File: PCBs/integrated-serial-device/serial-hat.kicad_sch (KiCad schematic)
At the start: 24 parts, among them CN1 Modem port, CN2 Modem out 3, CN3 Printer port, J1 Rpi headers, J2 Conn_01x03_Pin, K1 Quicktake, K2 ImageWriter, SW1 Modem To Proxy, SW2 Modem to Quicktake, SW3 Modem out 3, SW4 Printer out 3, SW5 Printer to Proxy, SW6 Printer to ImageWriter, SW7 SW_SPST, U1 MAX3232

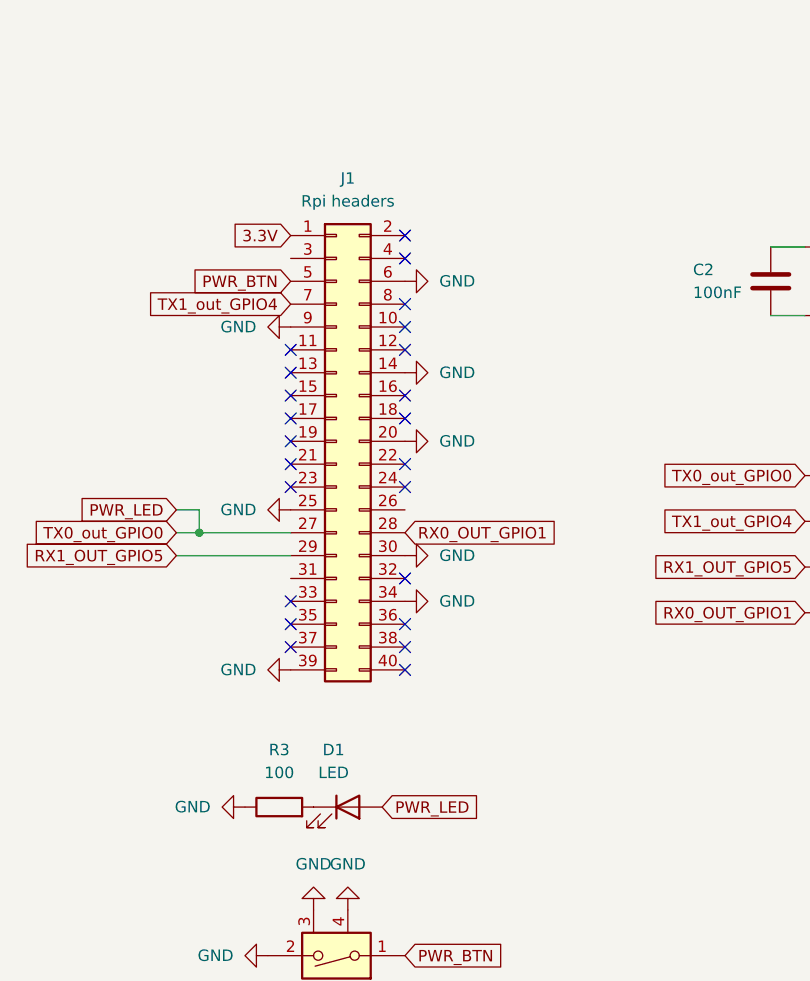
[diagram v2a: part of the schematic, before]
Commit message: Add fan headers
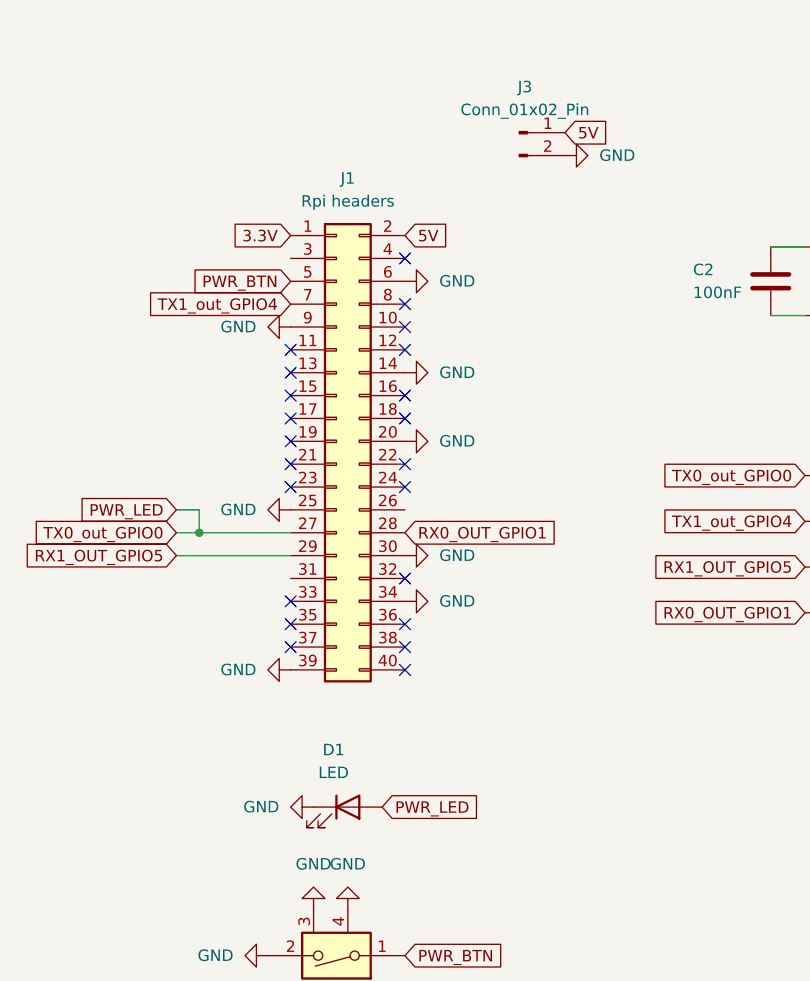
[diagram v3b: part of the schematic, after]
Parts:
- removed R3: 100, Resistor_SMD:R_0603_1608Metric, symbol Device:R
- added J3: Conn_01x02_Pin, Connector_PinHeader_2.54mm:PinHeader_1x02_P2.54mm_Vertical, symbol Connector:Conn_01x02_Pin
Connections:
- net GND: now also D1.1 (K), J3.2 (Pin_2)
- net 5V: now reaches J1.2 (Pin_2)
- net 5V: now also J3.1 (Pin_1)
- no-connect marks 59 -> 58
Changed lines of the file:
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@@
 	)
 	(no_connect
-		(at 100.33 38.1)
+		(at 100.33 40.64)
 	)
 	(no_connect
@@
 	)
 	(no_connect
-		(at 100.33 40.64)
-	)
-	(no_connect
 		(at 261.62 148.59)
 	)
@@
 		)
 	)
+	(global_label "5V"
+		(shape input)
+		(at 100.33 38.1 0)
+		(fields_autoplaced yes)
+		(effects
+			(font
+				(size 1.27 1.27)
+			)
+			(justify left)
+		)
+		(property "Intersheetrefs" "${INTERSHEET_REFS}"
+			(at 105.6133 38.1 0)
+			(effects
+				(font
+					(size 1.27 1.27)
+				)
+				(justify left)
+				(hide yes)
+			)
+		)
+	)
 	(global_label "IW_DSR"
 		(shape input)
@@
 		)
 	)
+	(global_label "5V"
+		(shape input)
+		(at 118.11 26.67 0)
+		(fields_autoplaced yes)
+		(effects
+			(font
+				(size 1.27 1.27)
+			)
+			(justify left)
+		)
+		(property "Intersheetrefs" "${INTERSHEET_REFS}"
+			(at 123.3933 26.67 0)
+			(effects
+				(font
+					(size 1.27 1.27)
+				)
+				(justify left)
+				(hide yes)
+			)
+		)
+	)
 	(global_label "IW_TX"
 		(shape input)
@@
 	)
 	(symbol
+		(lib_id "Connector:Conn_01x02_Pin")
+		(at 113.03 26.67 0)
+		(unit 1)
+		(exclude_from_sim no)
+		(in_bom yes)
+		(on_board yes)
+		(dnp no)
+		(fields_autoplaced yes)
+		(property "Reference" "J3"
+			(at 113.665 21.59 0)
+			(effects
+				(font
+					(size 1.27 1.27)
+				)
+			)
+		)
+		(property "Value" "Conn_01x02_Pin"
+			(at 113.665 24.13 0)
+			(effects
+				(font
+					(size 1.27 1.27)
+				)
+			)
+		)
+		(property "Footprint" "Connector_PinHeader_2.54mm:PinHeader_1x02_P2.54mm_Vertical"
+			(at 113.03 26.67 0)
+			(effects
+				(font
+					(size 1.27 1.27)
+				)
+				(hide yes)
+			)
+		)
+		(property "Datasheet" "~"
+			(at 113.03 26.67 0)
+			(effects
+				(font
+					(size 1.27 1.27)
+				)
+				(hide yes)
+			)
+		)
+		(property "Description" "Generic connector, single row, 01x02, script generated"
+			(at 113.03 26.67 0)
+			(effects
+				(font
+					(size 1.27 1.27)
+				)
+				(hide yes)
+			)
+		)
+		(pin "1"
+		)
+		(pin "2"
+		)
+		(instances
+			(project "serial-hat"
+				(path "/f30a5902-bf77-48c6-ab50-b8e2235ec207"
+					(reference "J3")
+					(unit 1)
+				)
+			)
+		)
+	)
+	(symbol
 		(lib_id "Device:R_US")
 		(at 189.23 74.93 90)
@@
 	)
 	(symbol
+		(lib_id "power:GND")
+		(at 118.11 29.21 90)
+		(unit 1)
+		(exclude_from_sim no)
+		(in_bom yes)
+		(on_board yes)
+		(dnp no)
+		(fields_autoplaced yes)
+		(property "Reference" "#PWR032"
+			(at 124.46 29.21 0)
+			(effects
+				(font
+					(size 1.27 1.27)
+				)
+				(hide yes)
+			)
+		)
+		(property "Value" "GND"
+			(at 121.92 29.2099 90)
+			(effects
+				(font
+					(size 1.27 1.27)
+				)
+				(justify right)
+			)
+		)
+		(property "Footprint" ""
+			(at 118.11 29.21 0)
+			(effects
+				(font
+					(size 1.27 1.27)
+				)
+				(hide yes)
+			)
+		)
+		(property "Datasheet" ""
+			(at 118.11 29.21 0)
+			(effects
+				(font
+					(size 1.27 1.27)
+				)
+				(hide yes)
+			)
+		)
+		(property "Description" "Power symbol creates a global label with name \"GND\" , ground"
+			(at 118.11 29.21 0)
+			(effects
+				(font
+					(size 1.27 1.27)
+				)
+				(hide yes)
+			)
+		)
+		(pin "1"
+		)
+		(instances
+			(project "serial-hat"
+				(path "/f30a5902-bf77-48c6-ab50-b8e2235ec207"
+					(reference "#PWR032")
+					(unit 1)
+				)
+			)
+		)
+	)
+	(symbol
 		(lib_id "Device:C")
 		(at 140.97 43.18 0)
@@
 	)
 	(symbol
-		(lib_id "Device:R")
-		(at 86.36 101.6 90)
-		(unit 1)
-		(exclude_from_sim no)
-		(in_bom yes)
-		(on_board yes)
-		(dnp no)
-		(fields_autoplaced yes)
-		(property "Reference" "R3"
-			(at 86.36 95.25 90)
-			(effects
-				(font
-					(size 1.27 1.27)
-				)
-			)
-		)
-		(property "Value" "100"
-			(at 86.36 97.79 90)
-			(effects
-				(font
-					(size 1.27 1.27)
-				)
-			)
-		)
-		(property "Footprint" "Resistor_SMD:R_0603_1608Metric"
-			(at 86.36 103.378 90)
-			(effects
-				(font
-					(size 1.27 1.27)
-				)
-				(hide yes)
-			)
-		)
-		(property "Datasheet" "~"
-			(at 86.36 101.6 0)
-			(effects
-				(font
-					(size 1.27 1.27)
-				)
-				(hide yes)
-			)
-		)
-		(property "Description" "Resistor"
-			(at 86.36 101.6 0)
-			(effects
-				(font
-					(size 1.27 1.27)
-				)
-				(hide yes)
-			)
-		)
-		(property "LCSC" "C22775"
-			(at 86.36 101.6 90)
-			(effects
-				(font
-					(size 1.27 1.27)
-				)
-				(hide yes)
-			)
-		)
-		(pin "2"
-		)
-		(pin "1"
-		)
-		(instances
-			(project "serial-hat"
-				(path "/f30a5902-bf77-48c6-ab50-b8e2235ec207"
-					(reference "R3")
-					(unit 1)
-				)
-			)
-		)
-	)
-	(symbol
 		(lib_id "power:GND")
 		(at 255.27 142.24 90)
@@
 	(symbol
 		(lib_id "power:GND")
-		(at 82.55 101.6 270)
+		(at 90.17 101.6 270)
 		(unit 1)
 		(exclude_from_sim no)
@@
 		(fields_autoplaced yes)
 		(property "Reference" "#PWR029"
-			(at 76.2 101.6 0)
+			(at 83.82 101.6 0)
 			(effects
 				(font
@@
 		)
 		(property "Value" "GND"
-			(at 78.74 101.6001 90)
+			(at 86.36 101.6001 90)
 			(effects
 				(font
@@
 		)
 		(property "Footprint" ""
-			(at 82.55 101.6 0)
+			(at 90.17 101.6 0)
 			(effects
 				(font
@@
 		)
 		(property "Datasheet" ""
-			(at 82.55 101.6 0)
+			(at 90.17 101.6 0)
 			(effects
 				(font
@@
 		)
 		(property "Description" "Power symbol creates a global label with name \"GND\" , ground"
-			(at 82.55 101.6 0)
+			(at 90.17 101.6 0)
 			(effects
 				(font

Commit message: CISD ready
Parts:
- removed R1, R2: 3.3k, Resistor_SMD:R_0603_1608Metric, symbol Device:R_US
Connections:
- net A2_AUX_TTY_TX: now also U1.13 (R1IN)
- net A2_TTY_TX: now also U1.8 (R2IN)
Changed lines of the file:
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@@
 	(global_label "A2_AUX_TTY_TX"
 		(shape input)
-		(at 193.04 74.93 0)
-		(fields_autoplaced yes)
-		(effects
-			(font
-				(size 1.27 1.27)
-			)
-			(justify left)
-		)
-		(property "Intersheetrefs" "${INTERSHEET_REFS}"
-			(at 210.0556 74.93 0)
+		(at 185.42 74.93 0)
+		(fields_autoplaced yes)
+		(effects
+			(font
+				(size 1.27 1.27)
+			)
+			(justify left)
+		)
+		(property "Intersheetrefs" "${INTERSHEET_REFS}"
+			(at 202.4356 74.93 0)
 			(effects
 				(font
@@
 	(global_label "A2_TTY_TX"
 		(shape input)
-		(at 193.04 80.01 0)
-		(fields_autoplaced yes)
-		(effects
-			(font
-				(size 1.27 1.27)
-			)
-			(justify left)
-		)
-		(property "Intersheetrefs" "${INTERSHEET_REFS}"
-			(at 205.4594 80.01 0)
+		(at 185.42 80.01 0)
+		(fields_autoplaced yes)
+		(effects
+			(font
+				(size 1.27 1.27)
+			)
+			(justify left)
+		)
+		(property "Intersheetrefs" "${INTERSHEET_REFS}"
+			(at 197.8394 80.01 0)
 			(effects
 				(font
@@
 				(path "/f30a5902-bf77-48c6-ab50-b8e2235ec207"
 					(reference "J3")
-					(unit 1)
-				)
-			)
-		)
-	)
-	(symbol
-		(lib_id "Device:R_US")
-		(at 189.23 74.93 90)
-		(unit 1)
-		(exclude_from_sim no)
-		(in_bom yes)
-		(on_board yes)
-		(dnp no)
-		(property "Reference" "R1"
-			(at 187.452 72.898 90)
-			(effects
-				(font
-					(size 1.27 1.27)
-				)
-			)
-		)
-		(property "Value" "3.3k"
-			(at 192.278 72.898 90)
-			(effects
-				(font
-					(size 1.27 1.27)
-				)
-			)
-		)
-		(property "Footprint" "Resistor_SMD:R_0603_1608Metric"
-			(at 189.484 73.914 90)
-			(effects
-				(font
-					(size 1.27 1.27)
-				)
-				(hide yes)
-			)
-		)
-		(property "Datasheet" "~"
-			(at 189.23 74.93 0)
-			(effects
-				(font
-					(size 1.27 1.27)
-				)
-				(hide yes)
-			)
-		)
-		(property "Description" "Resistor, US symbol"
-			(at 189.23 74.93 0)
-			(effects
-				(font
-					(size 1.27 1.27)
-				)
-				(hide yes)
-			)
-		)
-		(property "LCSC" "C21190"
-			(at 189.23 74.93 90)
-			(effects
-				(font
-					(size 1.27 1.27)
-				)
-				(hide yes)
-			)
-		)
-		(pin "2"
-		)
-		(pin "1"
-		)
-		(instances
-			(project "serial-hat"
-				(path "/f30a5902-bf77-48c6-ab50-b8e2235ec207"
-					(reference "R1")
 					(unit 1)
 				)
@@
 					(unit 1)
 				)
-			)
-		)
-	)
-	(symbol
-		(lib_id "Device:R_US")
-		(at 189.23 80.01 90)
-		(unit 1)
-		(exclude_from_sim no)
-		(in_bom yes)
-		(on_board yes)
-		(dnp no)
-		(property "Reference" "R2"
-			(at 187.452 77.978 90)
-			(effects
-				(font
-					(size 1.27 1.27)
-				)
-			)
-		)
-		(property "Value" "3.3k"
-			(at 192.278 77.978 90)
-			(effects
-				(font
-					(size 1.27 1.27)
-				)
-			)
-		)
-		(property "Footprint" "Resistor_SMD:R_0603_1608Metric"
-			(at 189.484 78.994 90)
-			(effects
-				(font
-					(size 1.27 1.27)
-				)
-				(hide yes)
-			)
-		)
-		(property "Datasheet" "~"
-			(at 189.23 80.01 0)
-			(effects
-				(font
-					(size 1.27 1.27)
-				)
-				(hide yes)
-			)
-		)
-		(property "Description" "Resistor, US symbol"
-			(at 189.23 80.01 0)
-			(effects
-				(font
-					(size 1.27 1.27)
-				)
-				(hide yes)
-			)
-		)
-		(property "LCSC" "C21190"
-			(at 189.23 80.01 90)
-			(effects
-				(font
-					(size 1.27 1.27)
-				)
-				(hide yes)
-			)
-		)
-		(pin "2"
-		)
-		(pin "1"
-		)
-		(instances
-			(project "serial-hat"
-				(path "/f30a5902-bf77-48c6-ab50-b8e2235ec207"
-					(reference "R2")
-					(unit 1)
-				)

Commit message: Fix CISD Quicktake
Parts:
- removed J2: Conn_01x03_Pin, Connector_PinHeader_2.54mm:PinHeader_1x03_P2.54mm_Vertical, symbol Connector:Conn_01x03_Pin
- added SW8: SW_Slide_DPDT, DIN5:DPDT slide switch C7507433, symbol Switch:SW_Slide_DPDT
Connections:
- net IW_DTR: now also SW8.4 (A)
- net Quicktake_DTR: now also SW8.5 (B)
- net Quicktake_DTR_Modem: now also SW8.3 (C), SW8.6 (C)
- net Quicktake_DSR: now reaches K1.2
- net Quicktake_DSR: now also SW8.1 (A)
- net Quicktake_DSR_Modem: now reaches SW2.C1
- net Quicktake_DSR_Modem: now also SW8.2 (B)
- no-connect marks 58 -> 57
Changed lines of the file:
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@@
 	)
 	(junction
-		(at 146.05 127)
+		(at 151.13 130.81)
 		(diameter 0)
 		(color 0 0 0 0)
@@
 	)
 	(no_connect
-		(at 33.02 85.09)
-	)
-	(no_connect
 		(at 100.33 40.64)
 	)
@@
 	(wire
 		(pts
-			(xy 157.48 127) (xy 146.05 127)
-		)
-		(stroke
-			(width 0)
-			(type default)
-		)
-	)
-	(wire
-		(pts
-			(xy 146.05 127) (xy 143.51 127)
-		)
-		(stroke
-			(width 0)
-			(type default)
-		)
-	)
-	(wire
-		(pts
 			(xy 165.1 29.21) (xy 165.1 31.75)
 		)
@@
 	(wire
 		(pts
-			(xy 143.51 123.19) (xy 152.4 123.19)
-		)
-		(stroke
-			(width 0)
-			(type default)
-		)
-	)
-	(wire
-		(pts
 			(xy 77.47 71.12) (xy 87.63 71.12)
 		)
@@
 	(wire
 		(pts
-			(xy 154.94 123.19) (xy 154.94 129.54)
-		)
-		(stroke
-			(width 0)
-			(type default)
-		)
-	)
-	(wire
-		(pts
 			(xy 165.1 25.4) (xy 165.1 29.21)
 		)
@@
 	(wire
 		(pts
-			(xy 154.94 129.54) (xy 162.56 129.54)
-		)
-		(stroke
-			(width 0)
-			(type default)
-		)
-	)
-	(wire
-		(pts
 			(xy 185.42 59.69) (xy 198.12 59.69)
 		)
@@
 	(wire
 		(pts
-			(xy 77.47 68.58) (xy 77.47 71.12)
+			(xy 149.86 130.81) (xy 151.13 130.81)
 		)
 		(stroke
@@
 	(wire
 		(pts
-			(xy 140.97 39.37) (xy 144.78 39.37)
+			(xy 151.13 130.81) (xy 151.13 127)
 		)
 		(stroke
@@
 	(wire
 		(pts
-			(xy 146.05 133.35) (xy 162.56 133.35)
+			(xy 77.47 68.58) (xy 77.47 71.12)
 		)
 		(stroke
@@
 	(wire
 		(pts
-			(xy 261.62 30.48) (xy 280.67 30.48)
+			(xy 140.97 39.37) (xy 144.78 39.37)
 		)
 		(stroke
@@
 	(wire
 		(pts
-			(xy 146.05 127) (xy 146.05 133.35)
+			(xy 261.62 30.48) (xy 280.67 30.48)
 		)
 		(stroke
@@
 	(wire
 		(pts
-			(xy 280.67 21.59) (xy 280.67 30.48)
+			(xy 151.13 130.81) (xy 153.67 130.81)
 		)
 		(stroke
@@
 	(wire
 		(pts
-			(xy 157.48 123.19) (xy 157.48 127)
+			(xy 280.67 21.59) (xy 280.67 30.48)
 		)
 		(stroke
@@
 		)
 	)
+	(global_label "Quicktake_DSR"
+		(shape input)
+		(at 33.02 85.09 0)
+		(fields_autoplaced yes)
+		(effects
+			(font
+				(size 1.27 1.27)
+			)
+			(justify left)
+		)
+		(property "Intersheetrefs" "${INTERSHEET_REFS}"
+			(at 49.9147 85.09 0)
+			(effects
+				(font
+					(size 1.27 1.27)
+				)
+				(justify left)
+				(hide yes)
+			)
+		)
+	)
 	(global_label "Modem_RX_in"
 		(shape input)
@@
 		)
 	)
+	(global_label "Quicktake_DSR"
+		(shape input)
+		(at 163.83 140.97 0)
+		(fields_autoplaced yes)
+		(effects
+			(font
+				(size 1.27 1.27)
+			)
+			(justify left)
+		)
+		(property "Intersheetrefs" "${INTERSHEET_REFS}"
+			(at 180.7247 140.97 0)
+			(effects
+				(font
+					(size 1.27 1.27)
+				)
+				(justify left)
+				(hide yes)
+			)
+		)
+	)
 	(global_label "Modem_TX_out3"
 		(shape input)
@@
 	(global_label "Quicktake_DTR_Printer"
 		(shape input)
-		(at 143.51 127 180)
+		(at 149.86 130.81 180)
 		(fields_autoplaced yes)
 		(effects
@@
 		)
 		(property "Intersheetrefs" "${INTERSHEET_REFS}"
-			(at 119.4791 127 0)
+			(at 125.8291 130.81 0)
 			(effects
 				(font
@@
 		)
 	)
+	(global_label "Quicktake_DSR_Modem"
+		(shape input)
+		(at 261.62 44.45 0)
+		(fields_autoplaced yes)
+		(effects
+			(font
+				(size 1.27 1.27)
+			)
+			(justify left)
+		)
+		(property "Intersheetrefs" "${INTERSHEET_REFS}"
+			(at 286.0136 44.45 0)
+			(effects
+				(font
+					(size 1.27 1.27)
+				)
+				(justify left)
+				(hide yes)
+			)
+		)
+	)
 	(global_label "Modem_TX_in"
 		(shape input)
@@
 		)
 	)
+	(global_label "Quicktake_DTR_Modem"
+		(shape input)
+		(at 163.83 130.81 0)
+		(fields_autoplaced yes)
+		(effects
+			(font
+				(size 1.27 1.27)
+			)
+			(justify left)
+		)
+		(property "Intersheetrefs" "${INTERSHEET_REFS}"
+			(at 187.9817 130.81 0)
+			(effects
+				(font
+					(size 1.27 1.27)
+				)
+				(justify left)
+				(hide yes)
+			)
+		)
+	)
 	(global_label "Modem_DTR_in"
 		(shape input)
@@
 	(global_label "IW_DTR"
 		(shape input)
-		(at 162.56 133.35 0)
+		(at 151.13 127 90)
 		(fields_autoplaced yes)
 		(effects
@@
 		)
 		(property "Intersheetrefs" "${INTERSHEET_REFS}"
-			(at 172.0766 133.35 0)
+			(at 151.13 117.4834 90)
 			(effects
 				(font
@@
 		)
 	)
+	(global_label "Quicktake_DSR_Modem"
+		(shape input)
+		(at 163.83 135.89 0)
+		(fields_autoplaced yes)
+		(effects
+			(font
+				(size 1.27 1.27)
+			)
+			(justify left)
+		)
+		(property "Intersheetrefs" "${INTERSHEET_REFS}"
+			(at 188.2236 135.89 0)
+			(effects
+				(font
+					(size 1.27 1.27)
+				)
+				(justify left)
+				(hide yes)
+			)
+		)
+	)
 	(global_label "IW_TX"
 		(shape input)
@@
 	(global_label "Quicktake_DTR"
 		(shape input)
-		(at 162.56 129.54 0)
+		(at 153.67 135.89 180)
 		(fields_autoplaced yes)
 		(effects
@@
 				(size 1.27 1.27)
 			)
-			(justify left)
+			(justify right)
 		)
 		(property "Intersheetrefs" "${INTERSHEET_REFS}"
-			(at 179.2128 129.54 0)
+			(at 137.0172 135.89 0)
 			(effects
 				(font
 					(size 1.27 1.27)
 				)
-				(justify left)
+				(justify right)
 				(hide yes)
 			)
@@
 	(global_label "Quicktake_DTR_Modem"
 		(shape input)
-		(at 143.51 123.19 180)
+		(at 153.67 140.97 180)
 		(fields_autoplaced yes)
 		(effects
@@
 		)
 		(property "Intersheetrefs" "${INTERSHEET_REFS}"
-			(at 119.3583 123.19 0)
+			(at 129.5183 140.97 0)
 			(effects
 				(font
@@
 	)
 	(symbol
+		(lib_id "Switch:SW_Slide_DPDT")
+		(at 158.75 135.89 180)
+		(unit 1)
+		(exclude_from_sim no)
+		(in_bom yes)
+		(on_board yes)
+		(dnp no)
+		(fields_autoplaced yes)
+		(property "Reference" "SW8"
+			(at 157.4799 129.54 90)
+			(effects
+				(font
+					(size 1.27 1.27)
+				)
+				(justify right)
+			)
+		)
+		(property "Value" "SW_Slide_DPDT"
+			(at 160.0199 129.54 90)
+			(effects
+				(font
+					(size 1.27 1.27)
+				)
+				(justify right)
+			)
+		)
+		(property "Footprint" "DIN5:DPDT slide switch C7507433"
+			(at 144.78 140.97 0)
+			(effects
+				(font
+					(size 1.27 1.27)
+				)
+				(hide yes)
+			)
+		)
+		(property "Datasheet" "~"
+			(at 158.75 135.89 0)
+			(effects
+				(font
+					(size 1.27 1.27)
+				)
+				(hide yes)
+			)
+		)
+		(property "Description" "Slide Switch, dual pole double throw"
+			(at 158.75 135.89 0)
+			(effects
+				(font
+					(size 1.27 1.27)
+				)
+				(hide yes)
+			)
+		)
+		(pin "1"
+		)
+		(pin "4"
+		)
+		(pin "2"
+		)
+		(pin "3"
+		)
+		(pin "6"
+		)
+		(pin "5"
+		)
+		(instances
+			(project "serial-hat"
+				(path "/f30a5902-bf77-48c6-ab50-b8e2235ec207"
+					(reference "SW8")
+					(unit 1)
+				)
+			)
+		)
+	)
+	(symbol
 		(lib_id "power:GND")
 		(at 205.74 52.07 90)
@@
 					(unit 1)
 				)
-			)
-		)
-	)
-	(symbol
-		(lib_id "Connector:Conn_01x03_Pin")
-		(at 154.94 118.11 270)
-		(unit 1)
-		(exclude_from_sim no)
-		(in_bom yes)
-		(on_board yes)
-		(dnp no)
-		(fields_autoplaced yes)
-		(property "Reference" "J2"
-			(at 154.94 113.03 90)
-			(effects
-				(font
-					(size 1.27 1.27)
-				)
-			)
-		)
-		(property "Value" "Conn_01x03_Pin"
-			(at 154.94 115.57 90)
-			(effects
-				(font
-					(size 1.27 1.27)
-				)
-			)
-		)
-		(property "Footprint" "Connector_PinHeader_2.54mm:PinHeader_1x03_P2.54mm_Vertical"
-			(at 154.94 118.11 0)
-			(effects
-				(font
-					(size 1.27 1.27)
-				)
-				(hide yes)
-			)
-		)
-		(property "Datasheet" "~"
-			(at 154.94 118.11 0)
-			(effects
-				(font
-					(size 1.27 1.27)
-				)
-				(hide yes)
-			)
-		)
-		(property "Description" "Generic connector, single row, 01x03, script generated"
-			(at 154.94 118.11 0)
-			(effects
-				(font
-					(size 1.27 1.27)
-				)
-				(hide yes)
-			)
-		)
-		(pin "1"
-		)
-		(pin "2"
-		)
-		(pin "3"
-		)
-		(instances
-			(project "serial-hat"
-				(path "/f30a5902-bf77-48c6-ab50-b8e2235ec207"
-					(reference "J2")
-					(unit 1)
-				)
